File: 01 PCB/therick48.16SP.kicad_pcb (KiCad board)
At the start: 2 copper layers, 308.9 x 75.8 mm, 173 parts, among them J1 TYPE-C-31-M12_13, J2 AVR-ISP-6_mod, K1 KEYSW, K10 KEYSW, K11 KEYSW, K12 KEYSW, K13 KEYSW, K14 KEYSW, K15 KEYSW, K16 KEYSW, K17 KEYSW, K18 KEYSW, K19 KEYSW, K2 KEYSW, K20 KEYSW, K21 KEYSW, K22 KEYSW, K23 KEYSW, K24 KEYSW, K25 KEYSW, K26 KEYSW, K27 KEYSW, K28 KEYSW, K29 KEYSW, K3 KEYSW, K30 KEYSW, K31 KEYSW, K32 KEYSW, K33 KEYSW, K34 KEYSW, K35 KEYSW, K36 KEYSW, K37 KEYSW, K38 KEYSW, K39 KEYSW, K4 KEYSW, K40 KEYSW, K41 KEYSW, K42 KEYSW, K43 KEYSW, K44 KEYSW, K45 KEYSW, K46 KEYSW, K47 KEYSW, K48 KEYSW, K49 KEYSW, K5 KEYSW, K50 KEYSW, K51 KEYSW, K52 KEYSW, K53 KEYSW, K54 KEYSW, K55 KEYSW, K56 KEYSW, K57 KEYSW, K58 KEYSW, K59 KEYSW, K6 KEYSW, K60 KEYSW, K61 KEYSW, K62 KEYSW, K63 KEYSW, K64 KEYSW, K7 KEYSW, K8 KEYSW, K9 KEYSW, SW1 SW_PUSH, U1 ATMEGA32U4, U2 HOLE, U3 USBLC6-2SC6, U4 HOLE, U5 HOLE, U6 HOLE, U7 HOLE, U8 HOLE, Y1 16MHz

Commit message: Add power LED
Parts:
- added LED1: LED, LED_SMD:LED_0805_2012Metric_Pad1.15x1.40mm_HandSolder, B.Cu at (162.6, 61.6)
- added R4: 1K, Resistor_SMD:R_0805_2012Metric_Pad1.15x1.40mm_HandSolder, B.Cu at (165.6, 61.6)
- added U9: HOLE, Symbol:OSHW-Logo2_9.8x8mm_SilkScreen, B.Cu at (145.5, 101.7)
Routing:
- net VCC: track 214.0 -> 217.5 mm
- net Net-(LED1-Pad2): track 0.00 -> 3.05 mm

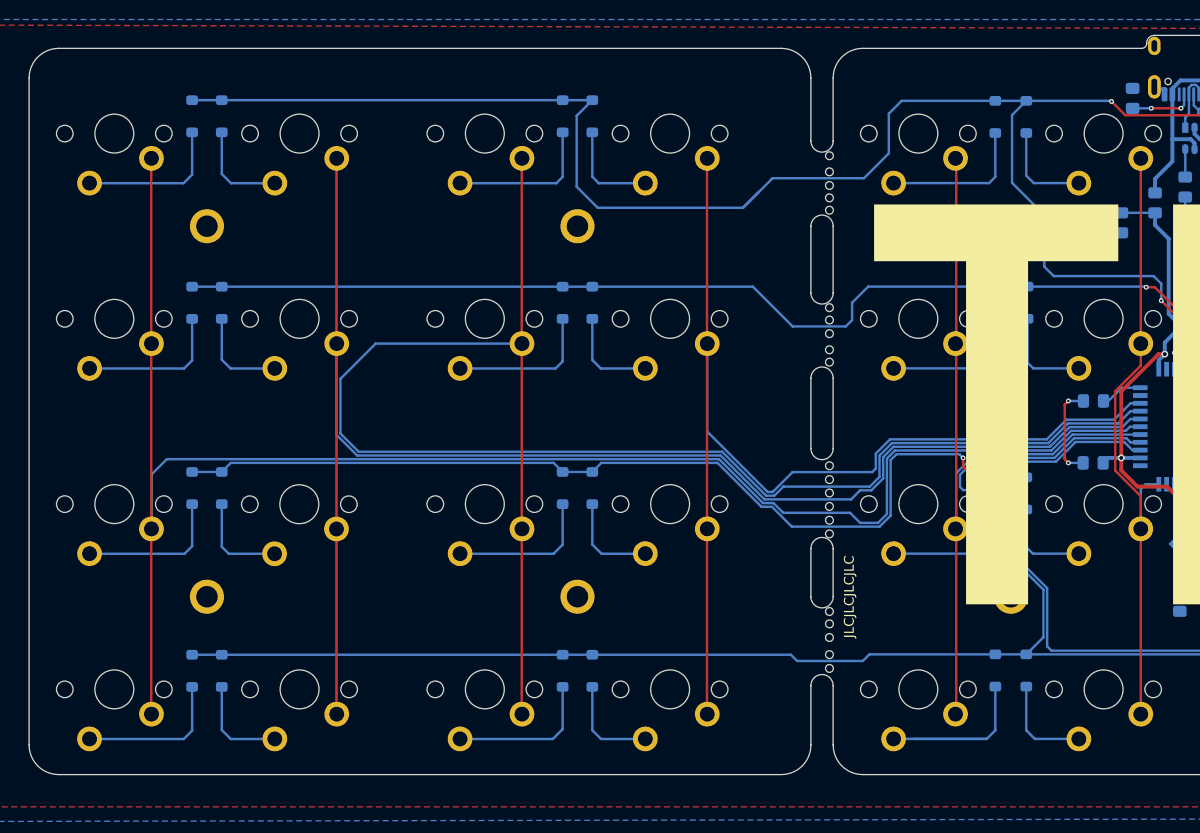
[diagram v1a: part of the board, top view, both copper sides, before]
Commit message: Made 2 columns able to be broken away
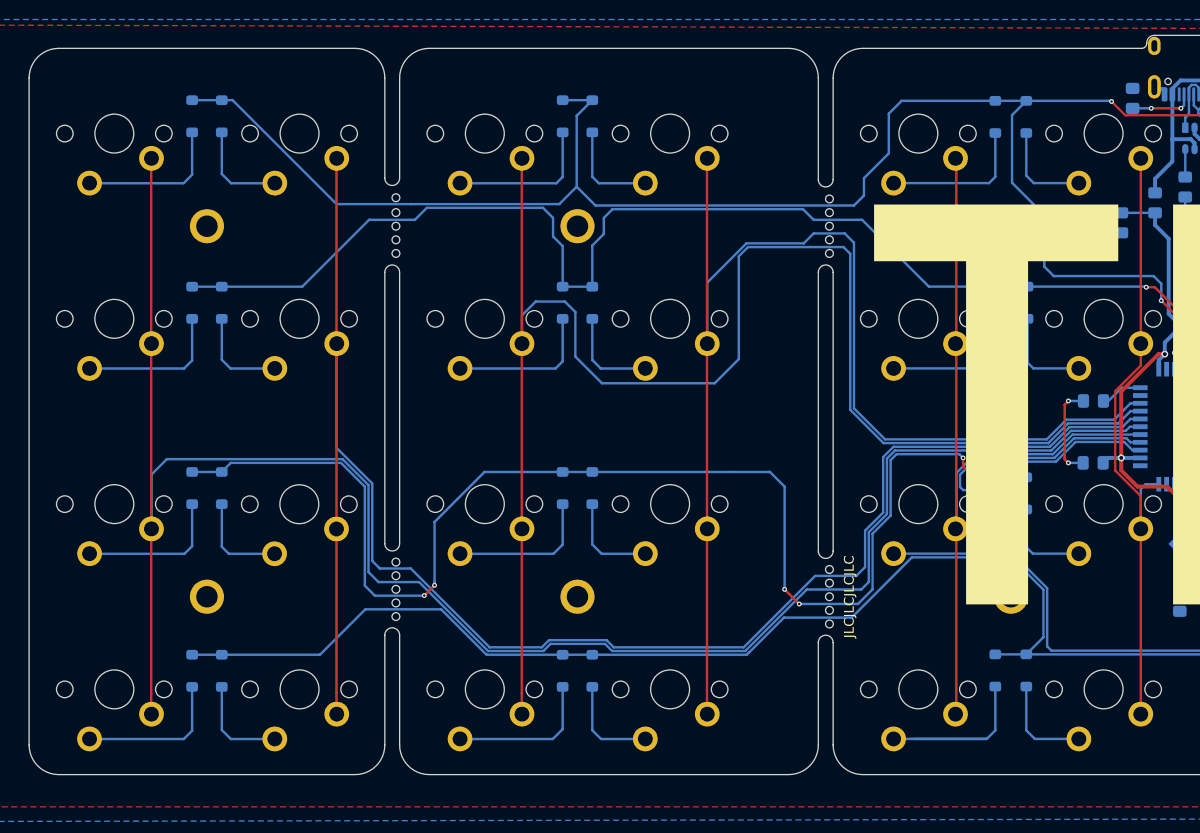
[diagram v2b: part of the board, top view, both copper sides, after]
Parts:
- U9: footprint Symbol:OSHW-Logo2_9.8x8mm_SilkScreen -> Symbol:OSHW-Logo2_14.6x12mm_SilkScreen
- moved U9 103.8 mm to (249.3, 99.2)
- moved U6 45.8 mm to (91.2, 61.9)
- moved U7 45.5 mm to (91.2, 99.2)
- moved U5 4.18 mm to (135.7, 99.9)
- moved U4 4.18 mm to (135.7, 61.9)
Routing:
- net row2: track 339.1 -> 374.7 mm, vias 2 -> 6
- net col13: track 156.2 -> 179.1 mm
- net col12: track 174.8 -> 194.5 mm
- net row1: track 292.9 -> 308.8 mm
- net col15: track 117.7 -> 130.0 mm
- net col14: track 172.3 -> 161.1 mm
- net row3: track 321.3 -> 330.1 mm
- net row0: track 339.2 -> 344.3 mm
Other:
- outline, holes or cut-outs redrawn
- board text added: "github.com/dierickdie"
- board text added: "therick48.16SP Rev 1.0"
- board text removed: "PCB Rev 1.0"
- board text removed: "therick48.16SP"

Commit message: Added breakaway section, added rotary encoder support
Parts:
- added H19: MountingHole, random-keyboard-parts:Generic-Mounthole, F.Cu at (109.8, 99.9)
- added H20: MountingHole, random-keyboard-parts:Generic-Mounthole, F.Cu at (109.8, 61.9)
- added SW2: Rotary_Encoder_Switch, Keebio-Parts:RotaryEncoder_EC11, F.Cu at (119.3, 52.4)
- added U10: HOLE, Keeb_footprints:MouseBite_IPC7351, F.Cu at (110.2, 72.2)
- added U11: HOLE, Keeb_footprints:MouseBite_IPC7351, F.Cu at (110.2, 89.7)
- moved H8 19.0 mm to (128.8, 61.9)
- moved H10 19.0 mm to (128.8, 99.9)
- moved D51 17.1 mm to (99.2, 65.2)
- moved D52 14.7 mm to (114.0, 65.2)
- moved D55 13.7 mm to (95.4, 65.2)
- moved D59 11.5 mm to (97.8, 84.1)
- moved D63 11.4 mm to (97.8, 103.1)
- moved D56 7.65 mm to (117.4, 65.2)
- moved D60 7.06 mm to (116.6, 84.1)
- moved D64 6.95 mm to (116.7, 103.1)
- moved U7 0.76 mm to (91.2, 99.9)
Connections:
- U1 pad 20: (no net) -> EncB
- U1 pad 21: (no net) -> EncA
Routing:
- net EncB: track 0.00 -> 122.6 mm, vias 0 -> 2
- net EncA: track 0.00 -> 115.8 mm, vias 0 -> 2
- net row2: track 374.7 -> 429.2 mm
- net row3: track 330.1 -> 345.6 mm
- net col14: track 161.1 -> 146.0 mm, vias 0 -> 2
- net col13: track 179.1 -> 193.6 mm
- net col12: track 194.5 -> 206.3 mm
- net col11: track 376.0 -> 385.0 mm, vias 1 -> 0
- net row0: track 344.3 -> 351.1 mm
- net col0: track 83.5 -> 77.6 mm, vias 0 -> 1
- net Net-(D63-Pad2): track 15.3 -> 9.49 mm
- net Net-(D59-Pad2): track 15.1 -> 9.80 mm
- net Net-(D25-Pad2): track 14.6 -> 19.5 mm
- net Net-(D51-Pad2): track 15.4 -> 10.7 mm, vias 0 -> 1
- net Net-(D55-Pad2): track 15.2 -> 11.1 mm
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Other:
- outline, holes or cut-outs redrawn
